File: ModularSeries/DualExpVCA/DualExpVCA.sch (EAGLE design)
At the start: 71 parts, among them IC1 LM13700_DIP, IC2 TL084P, IC3 TL084P, P1 455-1750-1-ND, P2 455-1750-1-ND, Q1 2N3906, Q2 2N3906, Q3 2N3906, Q4 2N3906

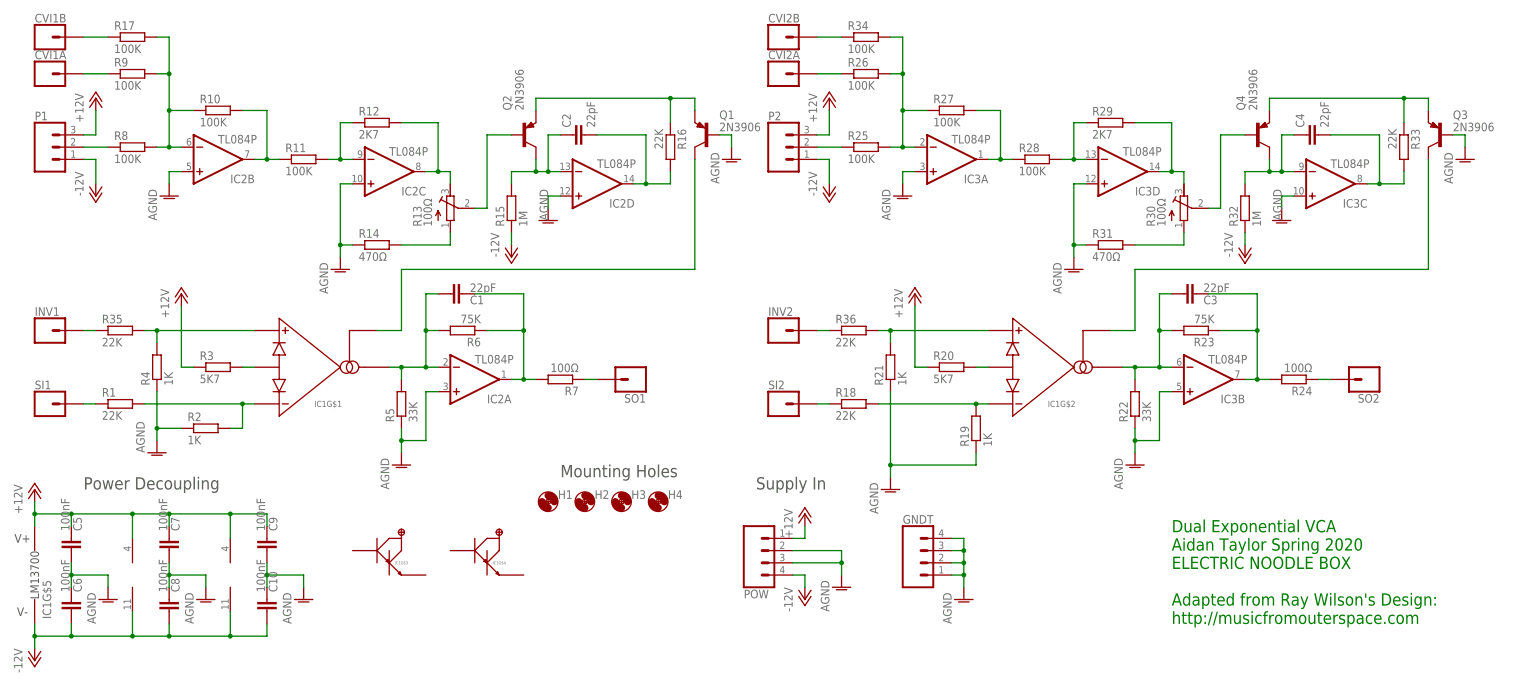
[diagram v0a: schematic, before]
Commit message: All PCBs now use unified library, Eagle library added
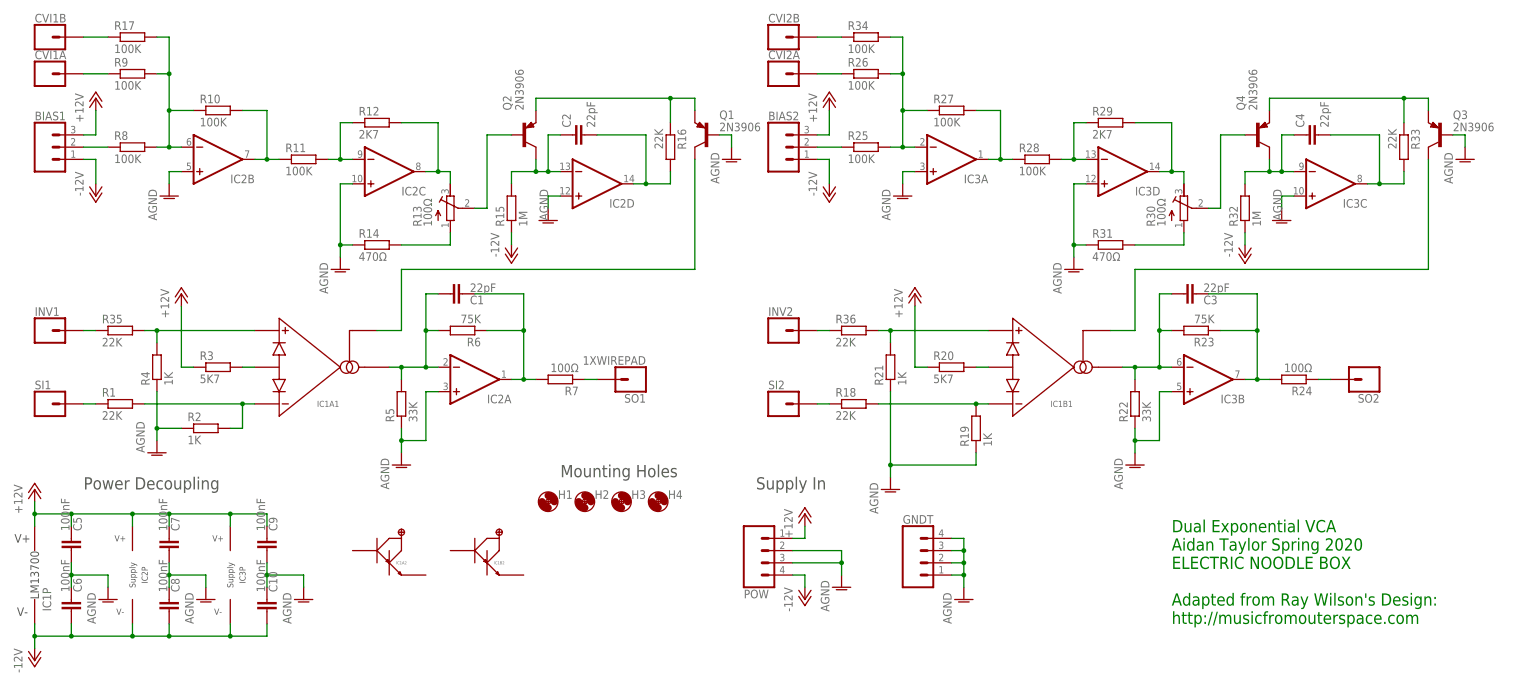
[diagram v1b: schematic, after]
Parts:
- removed P1, P2: 455-1750-1-ND, SparkFun-Connectors:CONN_03
- added BIAS1, BIAS2: 3XWIREPAD, ElectricNoodleBox:3XWIREPAD
- CVI1A, CVI1B, CVI2A, CVI2B, INV1, INV2, SI1, SI2, SO1, SO2: value (none) -> 1XWIREPAD; device SparkFun-Connectors:CONN_01 -> ElectricNoodleBox:1XWIREPAD
- GNDT: value (none) -> 4XWIREPAD; device SparkFun-Connectors:CONN_04 -> ElectricNoodleBox:4XWIREPAD
- IC1: device ElectricNoodleBox2018:LM13700_DIP -> ElectricNoodleBox:LM13700_DIP
- IC2, IC3: value TL084P -> TL0X4_DIP; device linear:TL084P -> ElectricNoodleBox:TL0X4_DIP
- POW: value (none) -> 4XMOLEX; device SparkFun-Connectors:CONN_04POLAR -> ElectricNoodleBox:4XMOLEX
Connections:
- net +12V: now also BIAS1.3, BIAS2.3, IC1P.V+; no longer IC1G$5.V+, P1.3, P2.3
- net -12V: now also BIAS1.1, BIAS2.1, IC1P.V-; no longer IC1G$5.V-, P1.1, P2.1
- net N$2: now also IC1A1.AMP+; no longer IC1G$1.AMP+
- net N$20: now also IC1A1.AMPBIAS; no longer IC1G$1.AMPBIAS
- net N$22: now also IC1B1.AMP+; no longer IC1G$2.AMP+
- net N$23: now also IC1B1.AMP-; no longer IC1G$2.AMP-
- net N$24: now also IC1B1.DIODES; no longer IC1G$2.DIODES
- net N$25: now also IC1B1.AMPOUT; no longer IC1G$2.AMPOUT
- net N$28: now also BIAS2.2; no longer P2.2
- net N$3: now also BIAS1.2; no longer P1.2
- net N$38: now also IC1B1.AMPBIAS; no longer IC1G$2.AMPBIAS
- net N$4: now also IC1A1.AMP-; no longer IC1G$1.AMP-
- net N$5: now also IC1A1.DIODES; no longer IC1G$1.DIODES
- net N$7: now also IC1A1.AMPOUT; no longer IC1G$1.AMPOUT
